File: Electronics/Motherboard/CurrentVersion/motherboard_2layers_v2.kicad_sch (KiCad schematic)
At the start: 83 parts, among them J1 Conn_02x10_Odd_Even, J2 USB_C_Receptacle_USB2.0_16P, J3 Micro_SD_Card_Det2, M1 AO3400A, M2 AO3400A, M3 AO3400A, SW1 SW_Push, U1 LY1576HVS-5, U2 STZ12F405RGTx, U3 AMS1117-3.3, U5 USBLC6-2SC6

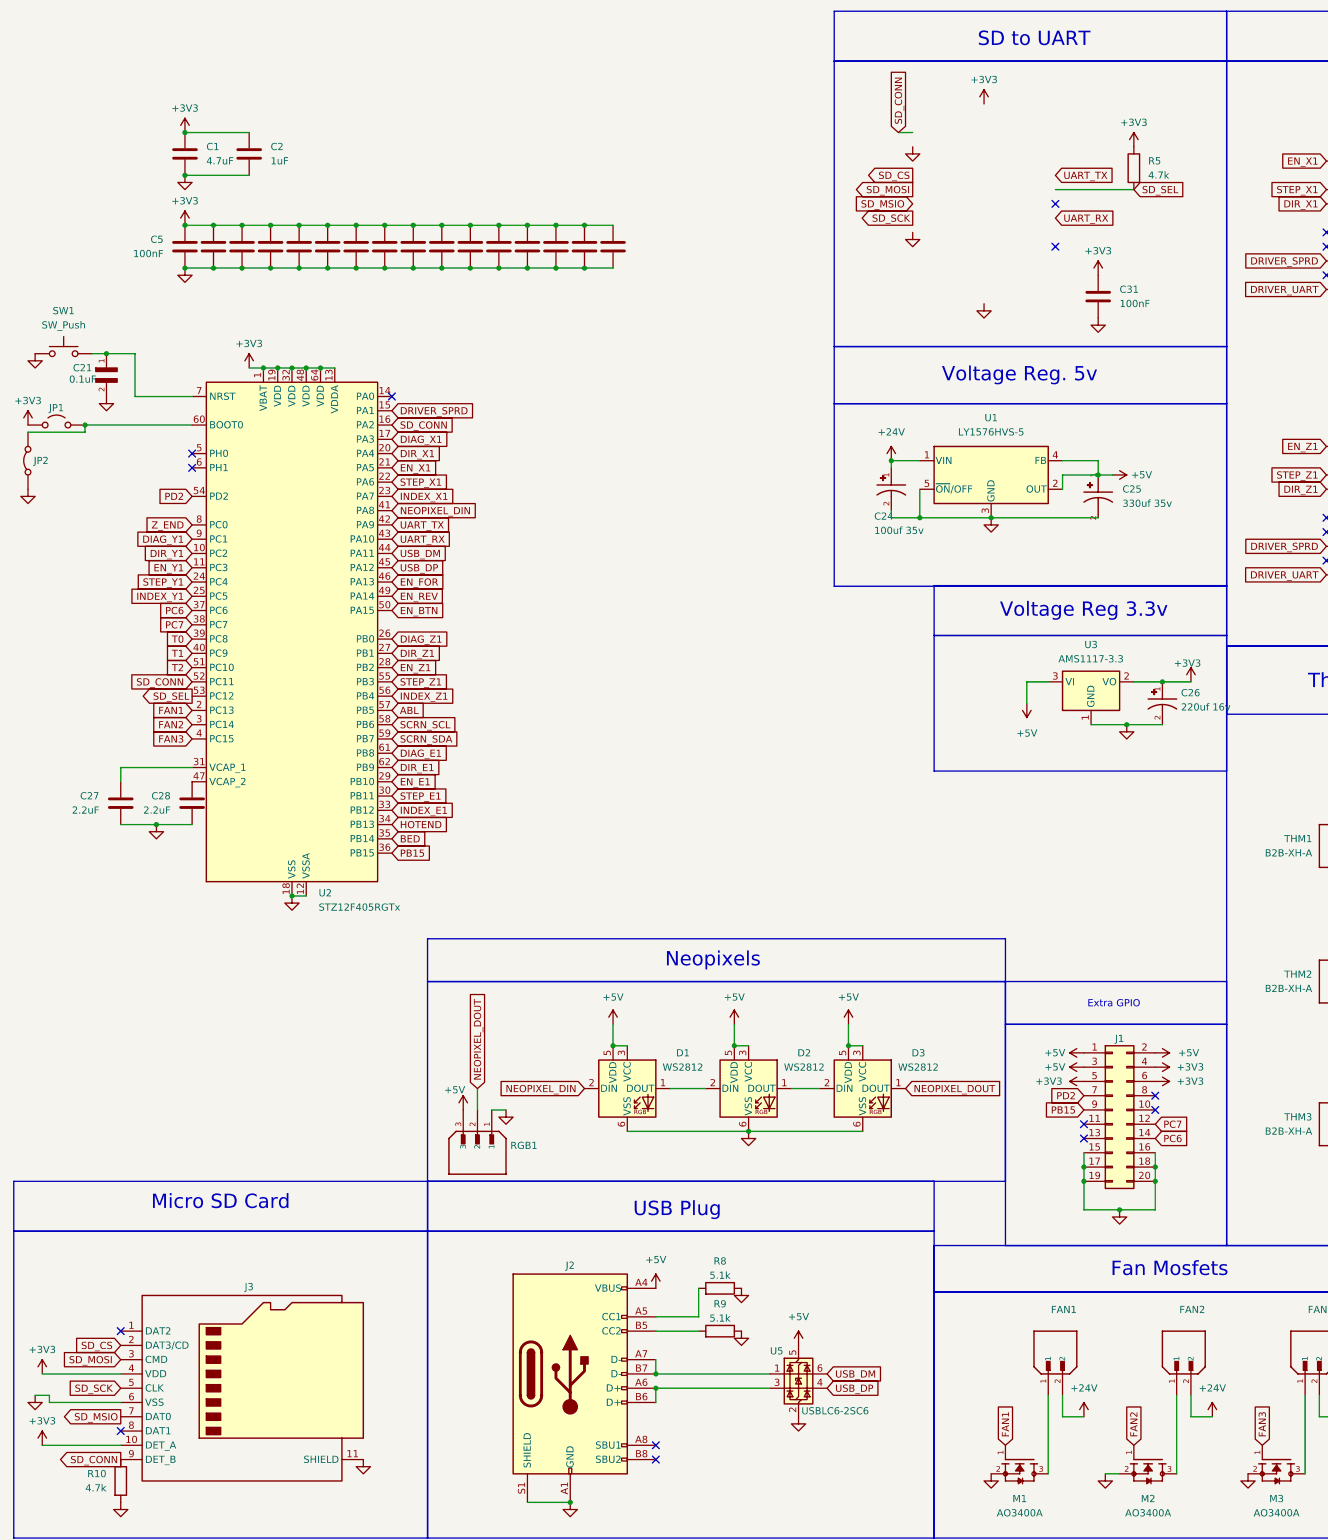
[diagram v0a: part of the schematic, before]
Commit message: Added stepper i2c expander and connected SD properly
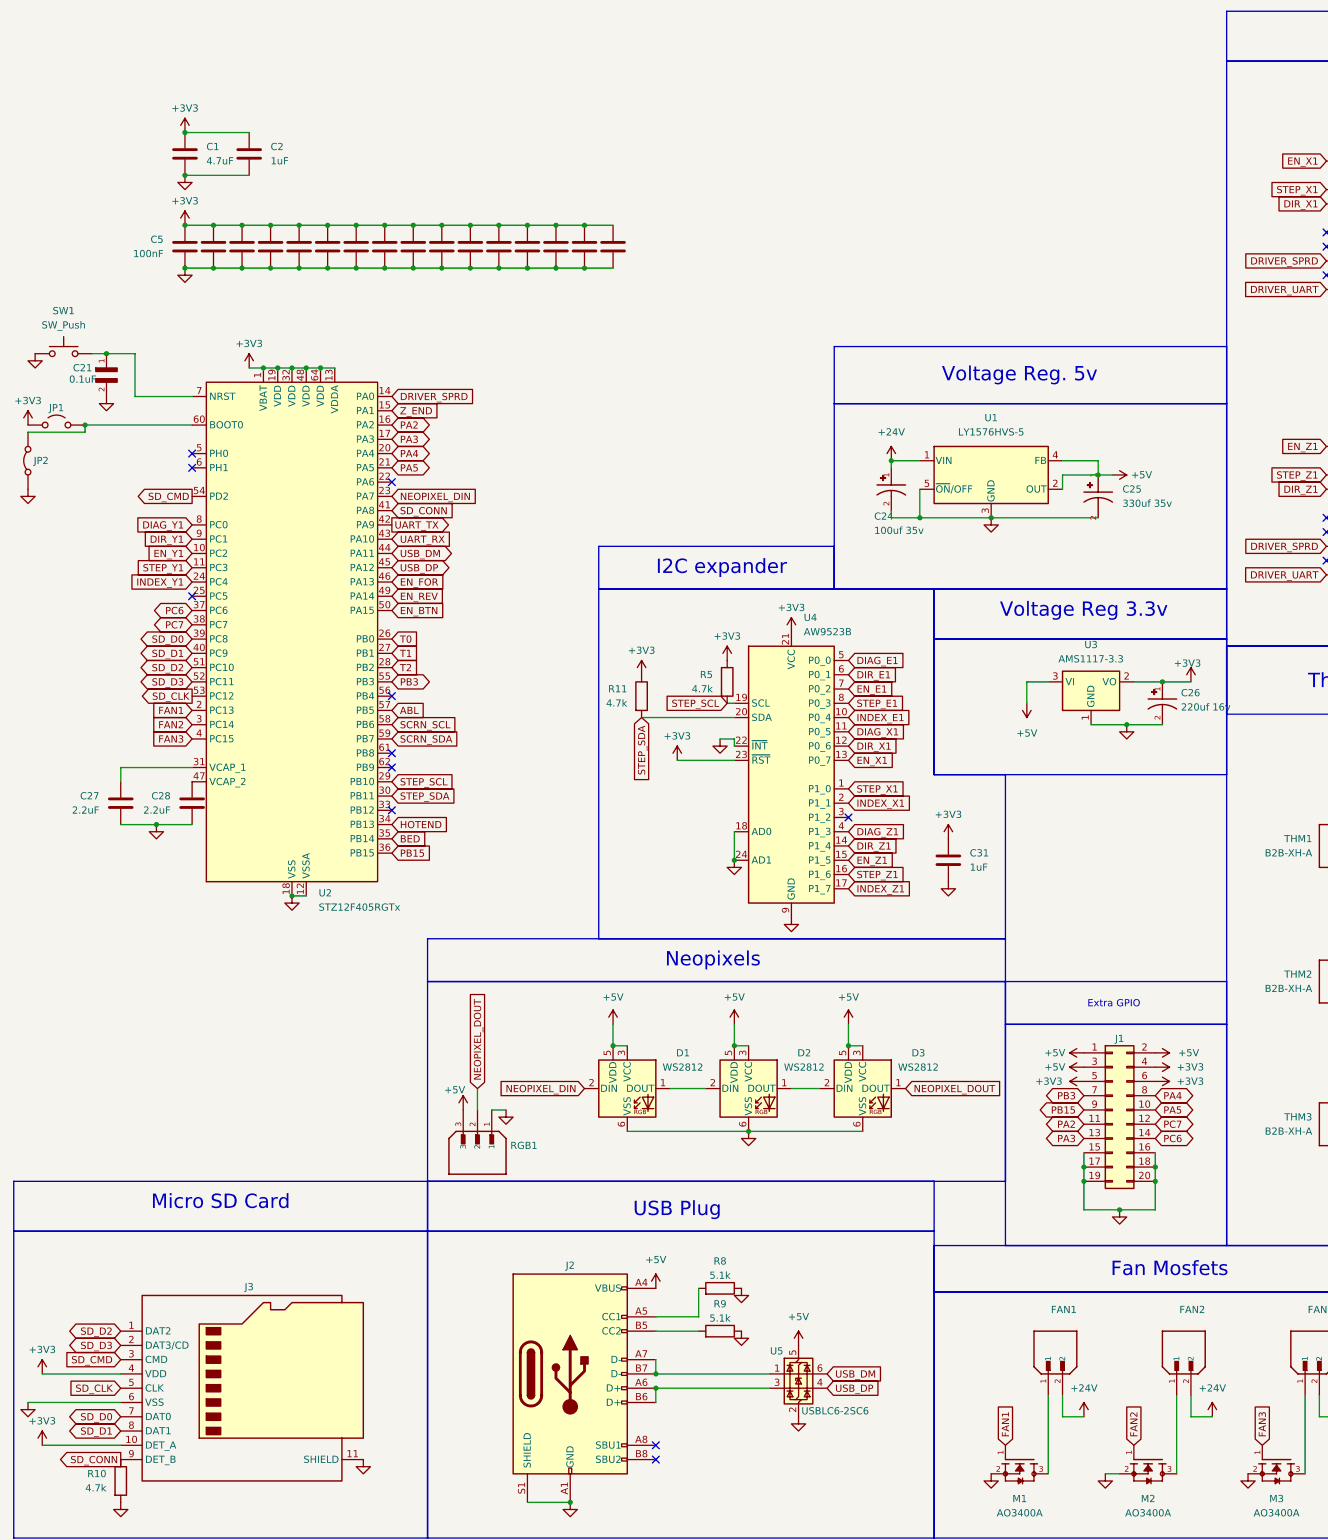
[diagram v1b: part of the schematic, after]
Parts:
- added R11: 4.7k, Resistor_SMD:R_1206_3216Metric, symbol Device:R
- added U4: AW9523B, Package_DFN_QFN:QFN-24-1EP_4x4mm_P0.5mm_EP2.7x2.7mm_ThermalVias, symbol Interface_Expansion:AW9523B
- C31: value 100nF -> 1uF; Part # TCC0402X7R104K160AT -> TCC0402X5R105K6R3AT
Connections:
- net +3V3: now also R11.1, U4.21 (VCC), U4.23 (~{RST})
- net DIAG_E1: now also U4.5 (P0_0); no longer U2.61 (PB8)
- net DIAG_X1: now also U4.11 (P0_5); no longer U2.17 (PA3)
- net DIAG_Y1: now also U2.8 (PC0); no longer U2.9 (PC1)
- net DIAG_Z1: now also U4.4 (P1_3); no longer U2.26 (PB0)
- net DIR_E1: now also U4.6 (P0_1); no longer U2.62 (PB9)
- net DIR_X1: now also U4.12 (P0_6); no longer U2.20 (PA4)
- net DIR_Y1: now also U2.9 (PC1); no longer U2.10 (PC2)
- net DIR_Z1: now also U4.14 (P1_4); no longer U2.27 (PB1)
- net DRIVER_SPRD: now also U2.14 (PA0); no longer U2.15 (PA1)
- net EN_E1: now also U4.7 (P0_2); no longer U2.29 (PB10)
- net EN_X1: now also U4.13 (P0_7); no longer U2.21 (PA5)
- net EN_Y1: now also U2.10 (PC2); no longer U2.11 (PC3)
- net EN_Z1: now also U4.15 (P1_5); no longer U2.28 (PB2)
- net GND: now also U4.18 (AD0), U4.22 (~{INT}), U4.24 (AD1), U4.25 (GND), U4.9 (GND)
- net INDEX_E1: now also U4.10 (P0_4); no longer U2.33 (PB12)
- net INDEX_X1: now also U4.2 (P1_1); no longer U2.23 (PA7)
- net INDEX_Y1: now also U2.24 (PC4); no longer U2.25 (PC5)
- net INDEX_Z1: now also U4.17 (P1_7); no longer U2.56 (PB4)
- net NEOPIXEL_DIN: now also U2.23 (PA7); no longer U2.41 (PA8)
- net SD_CONN: now also U2.41 (PA8); no longer U2.16 (PA2), U2.52 (PC11)
- net STEP_E1: now also U4.8 (P0_3); no longer U2.30 (PB11)
- net STEP_X1: now also U4.1 (P1_0); no longer U2.22 (PA6)
- net STEP_Y1: now also U2.11 (PC3); no longer U2.24 (PC4)
- net STEP_Z1: now also U4.16 (P1_6); no longer U2.55 (PB3)
- net T0: now also U2.26 (PB0); no longer U2.39 (PC8)
- net T1: now also U2.27 (PB1); no longer U2.40 (PC9)
- net T2: now also U2.28 (PB2); no longer U2.51 (PC10)
- net Z_END: now also U2.15 (PA1); no longer U2.8 (PC0)
- net SD_D2: now reaches J3.1 (DAT2)
- net SD_D2: now also U2.51 (PC10)
- net SD_D1: now reaches J3.8 (DAT1)
- net SD_D1: now also U2.40 (PC9)
- net PA5: now reaches J1.10 (Pin_10)
- net PA5: now also U2.21 (PA5)
- net PA2: now reaches J1.11 (Pin_11)
- net PA2: now also U2.16 (PA2)
- net PA3: now reaches J1.13 (Pin_13)
- net PA3: now also U2.17 (PA3)
- net PA4: now reaches J1.8 (Pin_8)
- net PA4: now also U2.20 (PA4)
- net PD2 renamed PB3
- net PB3: now also U2.55 (PB3); no longer U2.54 (PD2)
- net SD_CS renamed SD_D3
- net SD_D3: now also U2.52 (PC11)
- net SD_MOSI renamed SD_CMD
- net SD_CMD: now also U2.54 (PD2)
- net SD_MSIO renamed SD_D0
- net SD_D0: now also U2.39 (PC8)
- net SD_SCK renamed SD_CLK
- net SD_CLK: now also U2.53 (PC12)
- net SD_SEL renamed STEP_SCL
- net STEP_SCL: now also U2.29 (PB10), U4.19 (SCL); no longer U2.53 (PC12)
- new net STEP_SDA: R11.2, U2.30 (PB11), U4.20 (SDA)
- no-connect marks 25 -> 23
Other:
- note added: "I2C expander"
- note removed: "SD to UART"

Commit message: I *think* that the schematic is done
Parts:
- removed ABL1, FAN2, FAN3, THM1, THM2, THM3, Z_END1: B2B-XH-A, B2B-XH-A:JST_B2B-XH-A, symbol B2B-XH-A:B2B-XH-A
- removed BED1, HOTEND1: 1751248, Phoenix 1751248:PHOENIX_1751248, symbol 1751248:1751248
- removed C21, C29, C30, C32: 0.1uF, GCM155R71H104KE02J:CAPC1005X55N, symbol GCM155R71H104KE02J:GCM155R71H104KE02J
- removed C22, C23, C24, C3, C4: 100uf 35v, CAP_EEEFT1V101AP, symbol EEEFT1V101AP:EEEFT1V101AP
- removed C25: 330uf 35v, UWT1V101MCL1GS:CAPAE830X1000N, symbol UWT1V101MCL1GS:UWT1V101MCL1GS
- removed C26: 220uf 16v, EEEFN1C221XP:CAP_EEEFN1C221XP, symbol EEEFN1C221XP:EEEFN1C221XP
- removed FAN1: ~, B2B-XH-A:JST_B2B-XH-A, symbol B2B-XH-A:B2B-XH-A
- removed M1, M2, M3: AO3400A, AO3400A:SOT95P280X125-3N, symbol AO3400A:AO3400A
- removed MOTOR_E1, MOTOR_X1, MOTOR_Y1, MOTOR_Z1: B4B-XH-A, B4B-XH-A:JST_B4B-XH-A, symbol B4B-XH-A:B4B-XH-A
- removed Q1, Q2: ~, IRFH7440TRPBF:TRANS_FDMS86202, symbol IRFH7440TRPBF:IRFH7440TRPBF
- removed REN1: PEC11H-4015F-S0016, PinHeader:PinHeader_1x04_P2.54mm_Vertical, symbol PEC11H-4015F-S0016:PEC11H-4015F-S0016
- removed RGB1: B3B-XH-A, b3b-xh-a:JST_B3B-XH-A, symbol B3B-XH-A:B3B-XH-A
- removed S1, S2, S3, S4: TMC2209_SILENTSTEPSTICK, TMC2209_SILENTSTEPSTICK:MODULE_TMC2209_SILENTSTEPSTICK, symbol TMC2209_SILENTSTEPSTICK:TMC2209_SILENTSTEPSTICK
- removed SCRN1: SSD1306, PinHeader:PinHeader_1x04_P2.54mm_Vertical, symbol SSD1306-128x64_OLED:SSD1306
- added ABL1, THM1, THM2, THM3, Z_END1: Conn_01x02_Socket, Connector_JST:JST_XH_B2B-XH-A_1x02_P2.50mm_Vertical, symbol Connector:Conn_01x02_Socket
- added BED1, FAN1, FAN2, FAN3, HOTEND1: Conn_01x02_Socket, ad-hoc:ScrewTerminal-2pin-MKDS_1_2-3_5, symbol Connector:Conn_01x02_Socket
- added C19, C26, C27, C28: 0.1uF, Capacitor_SMD:C_0402_1005Metric, symbol Device:C
- added C20: 100uF, Capacitor_SMD:CP_Elec_6.3x5.9, symbol Device:C_Polarized
- added C21: 1000uF, Capacitor_Tantalum_SMD:CP_EIA-7343-43_Kemet-X, symbol Device:C_Polarized
- added C22: 22uF, Capacitor_Tantalum_SMD:CP_EIA-3216-18_Kemet-A, symbol Device:C_Polarized
- added D1: D_Schottky, Diode_THT:D_DO-201AD_P15.24mm_Horizontal, symbol Device:D_Schottky
- added J2: SSD1306, Connector_PinHeader_2.54mm:PinHeader_1x04_P2.54mm_Vertical, symbol Connector:Conn_01x04_Socket
- added L1: 100uH, Inductor_SMD:L_0805_2012Metric, symbol Device:L
- added MOTOR_E1, MOTOR_X1, MOTOR_Y1, MOTOR_Z1: Conn_01x04_Socket, Connector_JST:JST_XH_B4B-XH-A_1x04_P2.50mm_Vertical, symbol Connector:Conn_01x04_Socket
- added Q1, Q2: FDMS86202, Package_TO_SOT_SMD:TDSON-8-1, symbol Transistor_FET:FDMS86202
- added Q3, Q4, Q5: AO3400A, Package_TO_SOT_SMD:SOT-23, symbol Transistor_FET:AO3400A
- added RGB1: Conn_01x03_Socket, Connector_JST:JST_XH_B3B-XH-A_1x03_P2.50mm_Vertical, symbol Connector:Conn_01x03_Socket
- added ROT1: RotaryEncoder_Switch, ad-hoc:PEC11H-4xxxF-Sxxxx, symbol Device:RotaryEncoder_Switch
- added U1, U2, U4, U5: TMC2209_SilentStepStick, TMC2209-SilentStepStick:MODULE_TMC2209_SILENTSTEPSTICK, symbol SilentStepStick:TMC2209_SilentStepStick
- PWR1: footprint (none) -> ad-hoc:XT30PW-M
- renumbered C12 to C10, C13 to C11, C14 to C12, C15 to C13, C16 to C14, C17 to C15, C18 to C16, C19 to C17, C20 to C18, C27 to C23, C28 to C24, C31 to C25, C5 to C3, C6 to C4, C7 to C5, C8 to C6, C9 to C7, C10 to C8, C11 to C9, D1 to D2, D2 to D3, D3 to D4, J2 to J3, J3 to J4, R9 to R10, R10 to R11, R5 to R2, R11 to R3, R2 to R4, R3 to R5, R4 to R6, R6 to R7, R7 to R8, R8 to R9, U1 to U3, U2 to U6, U3 to U7, U4 to U8, U5 to U9
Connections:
- net +24V: now also BED1.2 (Pin_2), C20.1, FAN1.2 (Pin_2), FAN2.2 (Pin_2), FAN3.2 (Pin_2), HOTEND1.2 (Pin_2), U1.8 (VM), U2.8 (VM), U4.8 (VM), U5.8 (VM)
- net +3V3: now also C22.1, J2.2 (Pin_2), ROT1.C, ROT1.S2, U1.2 (VIO), U2.2 (VIO), U4.2 (VIO), U5.2 (VIO), Z_END1.2 (Pin_2)
- net +5V: now also C21.1, L1.2, RGB1.3 (Pin_3); no longer U3.2 (OUT)
- net ABL: now also ABL1.1 (Pin_1)
- net BED: now also Q2.4 (G)
- net DIAG_E1: now also U5.18 (DIAG)
- net DIAG_X1: now also U1.18 (DIAG)
- net DIAG_Y1: now also U2.18 (DIAG)
- net DIAG_Z1: now also U4.18 (DIAG)
- net DIR_E1: now also U5.9 (DIR)
- net DIR_X1: now also U1.9 (DIR)
- net DIR_Y1: now also U2.9 (DIR)
- net DIR_Z1: now also U4.9 (DIR)
- net DRIVER_SPRD: now also U1.13 (SPRD), U2.13 (SPRD), U4.13 (SPRD), U5.13 (SPRD)
- net DRIVER_UART: now also U1.12 (UART), U2.12 (UART), U4.12 (UART), U5.12 (UART)
- net EN_BTN: now also ROT1.S1
- net EN_E1: now also U5.16 (~{EN})
- net EN_FOR: now also ROT1.A
- net EN_REV: now also ROT1.B
- net EN_X1: now also U1.16 (~{EN})
- net EN_Y1: now also U2.16 (~{EN})
- net EN_Z1: now also U4.16 (~{EN})
- net FAN1: now also Q3.1 (G)
- net FAN2: now also Q4.1 (G)
- net FAN3: now also Q5.1 (G)
- net GND: now also ABL1.2 (Pin_2), C19.2, C20.2, C21.2, C22.2, C26.2, C27.2, C28.2, D1.2 (A), J2.1 (Pin_1), Q1.1 (S), Q1.2 (S), Q1.3 (S), Q2.1 (S), Q2.2 (S), Q2.3 (S), Q3.2 (S), Q4.2 (S), Q5.2 (S), RGB1.1 (Pin_1), THM1.1 (Pin_1), THM2.1 (Pin_1), THM3.1 (Pin_1), U1.1 (GND), U1.7 (GND), U2.1 (GND), U2.7 (GND), U4.1 (GND), U4.7 (GND), U5.1 (GND), U5.7 (GND)
- net HOTEND: now also Q1.4 (G)
- net INDEX_E1: now also U5.17 (INDEX)
- net INDEX_X1: now also U1.17 (INDEX)
- net INDEX_Y1: now also U2.17 (INDEX)
- net INDEX_Z1: now also U4.17 (INDEX)
- net NEOPIXEL_DOUT: now also RGB1.2 (Pin_2)
- net SCRN_SCL: now also J2.3 (Pin_3)
- net SCRN_SDA: now also J2.4 (Pin_4)
- net STEP_E1: now also U5.10 (STEP)
- net STEP_X1: now also U1.10 (STEP)
- net STEP_Y1: now also U2.10 (STEP)
- net STEP_Z1: now also U4.10 (STEP)
- net T0: now also C26.1, THM1.2 (Pin_2)
- net T1: now also C27.1, THM2.2 (Pin_2)
- net T2: now also C28.1, THM3.2 (Pin_2)
- net Z_END: now also Z_END1.1 (Pin_1)
- net at SW1.2, U6.7 (NRST): now also C19.1
- new net: MOTOR_E1.3 (Pin_3), U5.3 (M1B)
- new net: MOTOR_E1.1 (Pin_1), U5.4 (M1A)
- new net: MOTOR_E1.2 (Pin_2), U5.5 (M2A)
- new net: MOTOR_E1.4 (Pin_4), U5.6 (M2B)
- new net: BED1.1 (Pin_1), Q2.5 (D)
- new net: FAN1.1 (Pin_1), Q3.3 (D)
- new net: MOTOR_Y1.3 (Pin_3), U2.3 (M1B)
- new net: MOTOR_Y1.1 (Pin_1), U2.4 (M1A)
- new net: MOTOR_Y1.2 (Pin_2), U2.5 (M2A)
- new net: MOTOR_Y1.4 (Pin_4), U2.6 (M2B)
- new net: MOTOR_Z1.3 (Pin_3), U4.3 (M1B)
- new net: MOTOR_Z1.1 (Pin_1), U4.4 (M1A)
- new net: MOTOR_Z1.2 (Pin_2), U4.5 (M2A)
- new net: MOTOR_Z1.4 (Pin_4), U4.6 (M2B)
- new net: MOTOR_X1.1 (Pin_1), U1.4 (M1A)
- new net: MOTOR_X1.2 (Pin_2), U1.5 (M2A)
- new net: MOTOR_X1.3 (Pin_3), U1.3 (M1B)
- new net: MOTOR_X1.4 (Pin_4), U1.6 (M2B)
- new net: FAN2.1 (Pin_1), Q4.3 (D)
- new net: D1.1 (K), L1.1, U3.2 (OUT)
- new net: HOTEND1.1 (Pin_1), Q1.5 (D)
- new net: FAN3.1 (Pin_1), Q5.3 (D)
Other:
- moved on the sheet: R5, R8

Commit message: Finished schematic of motherboard2l2 and started PCB
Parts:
- F1: footprint RUEF900:FUSRR1015W81L2410T300H2900 -> ad-hoc:Fuse_RUEF900
- JP1: footprint (none) -> TestPoint:TestPoint_2Pads_Pitch2.54mm_Drill0.8mm; now left out of the parts list
- R10, R9: footprint RMCF0805JT5K10:RESC2012X65N -> Resistor_SMD:R_0805_2012Metric
- SW1: footprint (none) -> ad-hoc:SKHH_Button_TopPush; Part # (none) -> SKHHAMA010
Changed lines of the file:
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@@
 			)
 		)
-		(property "Footprint" "RMCF0805JT5K10:RESC2012X65N"
+		(property "Footprint" "Resistor_SMD:R_0805_2012Metric"
 			(at 138.43 241.808 90)
 			(effects
@@
 		(on_board yes)
 		(dnp no)
-		(fields_autoplaced yes)
 		(property "Reference" "SW1"
-			(at 21.59 66.04 0)
+			(at 21.59 69.088 0)
 			(effects
 				(font
@@
 					(size 1.27 1.27)
 				)
+				(hide yes)
 			)
 		)
-		(property "Footprint" ""
+		(property "Footprint" "ad-hoc:SKHH_Button_TopPush"
 			(at 21.59 68.58 0)
 			(effects
@@
 			)
 		)
-		(property "Description_1" ""
-			(at 21.59 73.66 0)
-			(effects
-				(font
-					(size 1.27 1.27)
-				)
-				(hide yes)
-			)
-		)
-		(property "DigiKey_Part_Number" ""
-			(at 21.59 73.66 0)
-			(effects
-				(font
-					(size 1.27 1.27)
-				)
-				(hide yes)
-			)
-		)
-		(property "MAXIMUM_PACKAGE_HEIGHT" ""
-			(at 21.59 73.66 0)
-			(effects
-				(font
-					(size 1.27 1.27)
-				)
-				(hide yes)
-			)
-		)
-		(property "Purchase-URL" ""
+		(property "Part #" "SKHHAMA010"
 			(at 21.59 73.66 0)
 			(effects
@@
 			)
 		)
-		(property "Footprint" "RUEF900:FUSRR1015W81L2410T300H2900"
+		(property "Footprint" "ad-hoc:Fuse_RUEF900"
 			(at 281.94 251.46 0)
 			(effects
@@
 			)
 		)
-		(property "Footprint" "RMCF0805JT5K10:RESC2012X65N"
+		(property "Footprint" "Resistor_SMD:R_0805_2012Metric"
 			(at 138.43 249.428 90)
 			(effects
@@
 		(unit 1)
 		(exclude_from_sim yes)
-		(in_bom yes)
+		(in_bom no)
 		(on_board yes)
 		(dnp no)
@@
 			)
 		)
-		(property "Footprint" ""
+		(property "Footprint" "TestPoint:TestPoint_2Pads_Pitch2.54mm_Drill0.8mm"
 			(at 20.32 86.36 0)
 			(effects

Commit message: Revert "Finished schematic of motherboard2l2 and started PCB"
This reverts commit ca30ac8bcea5a8143053b1259e3b8c4470504014.
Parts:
- F1: footprint ad-hoc:Fuse_RUEF900 -> RUEF900:FUSRR1015W81L2410T300H2900
- JP1: footprint TestPoint:TestPoint_2Pads_Pitch2.54mm_Drill0.8mm -> (none); now in the parts list
- R10, R9: footprint Resistor_SMD:R_0805_2012Metric -> RMCF0805JT5K10:RESC2012X65N
- SW1: footprint ad-hoc:SKHH_Button_TopPush -> (none); Part # SKHHAMA010 -> (none)
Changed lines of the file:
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@@
 			)
 		)
-		(property "Footprint" "Resistor_SMD:R_0805_2012Metric"
+		(property "Footprint" "RMCF0805JT5K10:RESC2012X65N"
 			(at 138.43 241.808 90)
 			(effects
@@
 		(on_board yes)
 		(dnp no)
+		(fields_autoplaced yes)
 		(property "Reference" "SW1"
-			(at 21.59 69.088 0)
+			(at 21.59 66.04 0)
 			(effects
 				(font
@@
 					(size 1.27 1.27)
 				)
-				(hide yes)
 			)
 		)
-		(property "Footprint" "ad-hoc:SKHH_Button_TopPush"
+		(property "Footprint" ""
 			(at 21.59 68.58 0)
 			(effects
@@
 			)
 		)
-		(property "Part #" "SKHHAMA010"
+		(property "Description_1" ""
+			(at 21.59 73.66 0)
+			(effects
+				(font
+					(size 1.27 1.27)
+				)
+				(hide yes)
+			)
+		)
+		(property "DigiKey_Part_Number" ""
+			(at 21.59 73.66 0)
+			(effects
+				(font
+					(size 1.27 1.27)
+				)
+				(hide yes)
+			)
+		)
+		(property "MAXIMUM_PACKAGE_HEIGHT" ""
+			(at 21.59 73.66 0)
+			(effects
+				(font
+					(size 1.27 1.27)
+				)
+				(hide yes)
+			)
+		)
+		(property "Purchase-URL" ""
 			(at 21.59 73.66 0)
 			(effects
@@
 			)
 		)
-		(property "Footprint" "ad-hoc:Fuse_RUEF900"
+		(property "Footprint" "RUEF900:FUSRR1015W81L2410T300H2900"
 			(at 281.94 251.46 0)
 			(effects
@@
 			)
 		)
-		(property "Footprint" "Resistor_SMD:R_0805_2012Metric"
+		(property "Footprint" "RMCF0805JT5K10:RESC2012X65N"
 			(at 138.43 249.428 90)
 			(effects
@@
 		(unit 1)
 		(exclude_from_sim yes)
-		(in_bom no)
+		(in_bom yes)
 		(on_board yes)
 		(dnp no)
@@
 			)
 		)
-		(property "Footprint" "TestPoint:TestPoint_2Pads_Pitch2.54mm_Drill0.8mm"
+		(property "Footprint" ""
 			(at 20.32 86.36 0)
 			(effects

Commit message: Fixed some stuff
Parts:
- removed ROT1: RotaryEncoder_Switch, ad-hoc:PEC11H-4xxxF-Sxxxx, symbol Device:RotaryEncoder_Switch
- added C29, C30, C31, C32: 100uF, Capacitor_SMD:CP_Elec_6.3x5.8, symbol Device:C_Polarized
- added J5: Encoder, Connector_JST:JST_XH_B5B-XH-A_1x05_P2.50mm_Vertical, symbol Connector:Conn_01x05_Socket
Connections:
- net +24V: now also C29.1, C30.1, C31.1, C32.1
- net +3V3: now also J5.1 (Pin_1), J5.4 (Pin_4)
- net EN_BTN: now also J5.2 (Pin_2)
- net EN_FOR: now also J5.3 (Pin_3)
- net EN_REV: now also J5.5 (Pin_5)
- net GND: now also C29.2, C30.2, C31.2, C32.2
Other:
- moved on the sheet: R8
